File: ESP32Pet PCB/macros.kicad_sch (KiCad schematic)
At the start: 6 parts, among them SW1 6x6mm Button, SW2 6x6mm Button, SW3 6x6mm Button

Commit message: Schematic Updated
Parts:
- added FID1, FID2, FID3: Fiducial, Fiducial:Fiducial_0.5mm_Mask1mm, symbol Mechanical:Fiducial
- added H1, H2, H3, H4: MountingHole, MountingHole:MountingHole_2.5mm_Pad, symbol Mechanical:MountingHole
- R2, R3, R4: footprint (none) -> Resistor_THT:R_Axial_DIN0204_L3.6mm_D1.6mm_P7.62mm_Horizontal

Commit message: Schematic complete, created custom footprints and symbols for TFT LCD
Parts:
- SW1, SW2, SW3: footprint SparkFun-Switch:Push_PTH_12x12mm -> Button_Switch_THT:SW_PUSH_6mm_H5mm
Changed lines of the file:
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@@
 			)
 		)
-		(property "Footprint" "SparkFun-Switch:Push_PTH_12x12mm"
+		(property "Footprint" "Button_Switch_THT:SW_PUSH_6mm_H5mm"
 			(at 91.44 92.71 0)
 			(effects
@@
 			)
 		)
-		(property "Footprint" "SparkFun-Switch:Push_PTH_12x12mm"
+		(property "Footprint" "Button_Switch_THT:SW_PUSH_6mm_H5mm"
 			(at 110.49 92.71 0)
 			(effects
@@
 			)
 		)
-		(property "Footprint" "SparkFun-Switch:Push_PTH_12x12mm"
+		(property "Footprint" "Button_Switch_THT:SW_PUSH_6mm_H5mm"
 			(at 128.27 92.71 0)
 			(effects

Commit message: PCB Design Complete
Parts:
- removed H1, H2, H3, H4: MountingHole, MountingHole:MountingHole_2.5mm_Pad, symbol Mechanical:MountingHole
- renumbered SW1 to DOWN, SW2 to SELECT, SW3 to UP

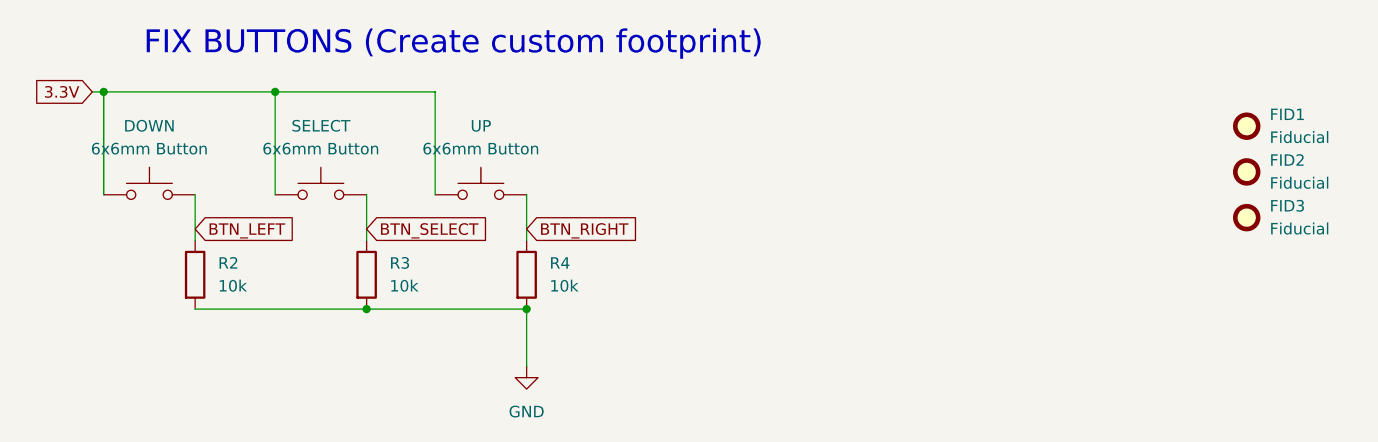
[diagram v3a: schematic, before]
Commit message: Updated ST7735S Footprint for bigger through holes
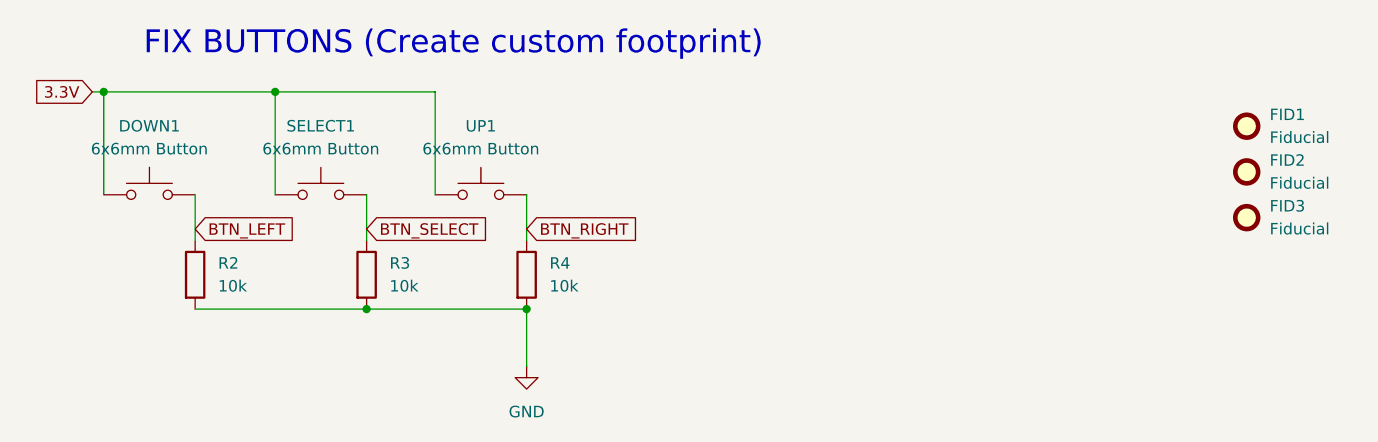
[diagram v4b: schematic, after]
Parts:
- renumbered DOWN to DOWN1, SELECT to SELECT1, UP to UP1
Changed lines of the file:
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@@
 		(dnp no)
 		(fields_autoplaced yes)
-		(property "Reference" "DOWN"
+		(property "Reference" "DOWN1"
 			(at 91.44 80.01 0)
 			(effects
@@
 			(project ""
 				(path "/397abc7c-300b-4d6f-9337-33290484b5ae/59951854-b551-47f5-ac04-53031cec35b0"
-					(reference "DOWN")
+					(reference "DOWN1")
 					(unit 1)
 				)
@@
 		(dnp no)
 		(fields_autoplaced yes)
-		(property "Reference" "SELECT"
+		(property "Reference" "SELECT1"
 			(at 110.49 80.01 0)
 			(effects
@@
 			(project "ESP32Pet"
 				(path "/397abc7c-300b-4d6f-9337-33290484b5ae/59951854-b551-47f5-ac04-53031cec35b0"
-					(reference "SELECT")
+					(reference "SELECT1")
 					(unit 1)
 				)
@@
 		(dnp no)
 		(fields_autoplaced yes)
-		(property "Reference" "UP"
+		(property "Reference" "UP1"
 			(at 128.27 80.01 0)
 			(effects
@@
 			(project "ESP32Pet"
 				(path "/397abc7c-300b-4d6f-9337-33290484b5ae/59951854-b551-47f5-ac04-53031cec35b0"
-					(reference "UP")
-					(unit 1)
-				)
+					(reference "UP1")
+					(unit 1)
+				)
